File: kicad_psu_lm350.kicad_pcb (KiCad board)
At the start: 2 copper layers, 28 parts, among them J1 AC Input, J2 AC Input, J3 DC +1.25 to +30V, J4 GND, J5 GND, J6 GND, J7 GND, U1 LM350_TO220

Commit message: Swapped pot pins, aligned schematic nets
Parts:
- moved D5 5.68 mm to (223.5, 48.3), turned to 90 degrees
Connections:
- C3 pad 2: Net-(C3-Pad2) -> Net-(C4-Pad1)
- C4 pad 1: Net-(C3-Pad2) -> Net-(C4-Pad1)
- D6 pad 2: Net-(C3-Pad2) -> Net-(C4-Pad1)
- R1 pad 2: Net-(C3-Pad2) -> Net-(C4-Pad1)
- R2 pad 1: Net-(C3-Pad2) -> Net-(C1-Pad2)
- R2 pad 3: Net-(C1-Pad2) -> Net-(C4-Pad1)
- U1 pad 1: Net-(C3-Pad2) -> Net-(C4-Pad1)
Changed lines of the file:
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@@
   (net 0 "")
   (net 1 "Net-(C5-Pad1)")
-  (net 2 "Net-(C3-Pad2)")
+  (net 2 "Net-(C4-Pad1)")
   (net 3 "Net-(C1-Pad2)")
   (net 4 "Net-(C1-Pad1)")
@@
     (fp_circle (center 1.25 0) (end 3.75 0) (layer "F.Fab") (width 0.1) (fill none))
     (pad "1" thru_hole rect (at 0 0) (size 1.6 1.6) (drill 0.8) (layers *.Cu *.Mask)
-      (net 2 "Net-(C3-Pad2)") (pintype "passive"))
+      (net 2 "Net-(C4-Pad1)") (pintype "passive"))
     (pad "2" thru_hole circle (at 2.5 0) (size 1.6 1.6) (drill 0.8) (layers *.Cu *.Mask)
       (net 3 "Net-(C1-Pad2)") (pintype "passive"))
@@
       (net 4 "Net-(C1-Pad1)") (pintype "passive"))
     (pad "2" thru_hole circle (at 5 0 180) (size 2 2) (drill 1) (layers *.Cu *.Mask)
-      (net 2 "Net-(C3-Pad2)") (pintype "passive"))
+      (net 2 "Net-(C4-Pad1)") (pintype "passive"))
     (model "${KICAD6_3DMODEL_DIR}/Capacitor_THT.3dshapes/C_Disc_D8.0mm_W5.0mm_P5.00mm.wrl"
       (offset (xyz 0 0 0))
@@
       (net 1 "Net-(C5-Pad1)") (pintype "passive"))
     (pad "2" thru_hole oval (at 10.16 0 270) (size 1.6 1.6) (drill 0.8) (layers *.Cu *.Mask)
-      (net 2 "Net-(C3-Pad2)") (pintype "passive"))
+      (net 2 "Net-(C4-Pad1)") (pintype "passive"))
     (model "${KICAD6_3DMODEL_DIR}/Resistor_THT.3dshapes/R_Axial_DIN0207_L6.3mm_D2.5mm_P10.16mm_Horizontal.wrl"
       (offset (xyz 0 0 0))
@@
     (fp_line (start -2.46 -3.15) (end -2.46 1.25) (layer "F.Fab") (width 0.1))
     (pad "1" thru_hole rect (at 0 0) (size 1.905 2) (drill 1.1) (layers *.Cu *.Mask)
-      (net 2 "Net-(C3-Pad2)") (pinfunction "ADJ") (pintype "input"))
+      (net 2 "Net-(C4-Pad1)") (pinfunction "ADJ") (pintype "input"))
     (pad "2" thru_hole oval (at 2.54 0) (size 1.905 2) (drill 1.1) (layers *.Cu *.Mask)
       (net 1 "Net-(C5-Pad1)") (pinfunction "VO") (pintype "power_out"))
@@
   )
   (footprint "Diode_THT:D_DO-41_SOD81_P10.16mm_Horizontal" (layer "F.Cu")
-    (at 220.98 43.18)
+    (at 223.52 48.26 90)
     (descr "Diode, DO-41_SOD81 series, Axial, Horizontal, pin pitch=10.16mm, , length*diameter=5.2*2.7mm^2, , http://www.diodes.com/_files/packages/DO-41%20(Plastic).pdf")
     (tags "Diode DO-41_SOD81 series Axial Horizontal pin pitch 10.16mm  length 5.2mm diameter 2.7mm")
@@
     (property "Sheetname" "")
     (attr through_hole)
-    (fp_text reference "D5" (at 5.08 -2.47) (layer "F.SilkS")
-      (effects (font (size 1 1) (thickness 0.15)))
-    )
-    (fp_text value "1N4007" (at 5.08 2.47) (layer "F.Fab")
-      (effects (font (size 1 1) (thickness 0.15)))
-    )
-    (fp_text user "K" (at 0 -2.1) (layer "F.SilkS")
-      (effects (font (size 1 1) (thickness 0.15)))
-    )
-    (fp_text user "K" (at 0 -2.1) (layer "F.Fab")
-      (effects (font (size 1 1) (thickness 0.15)))
-    )
-    (fp_text user "${REFERENCE}" (at 5.47 0) (layer "F.Fab")
+    (fp_text reference "D5" (at 5.08 -2.47 90) (layer "F.SilkS")
+      (effects (font (size 1 1) (thickness 0.15)))
+    )
+    (fp_text value "1N4007" (at 5.08 2.47 90) (layer "F.Fab")
+      (effects (font (size 1 1) (thickness 0.15)))
+    )
+    (fp_text user "K" (at 0 -2.1 90) (layer "F.SilkS")
+      (effects (font (size 1 1) (thickness 0.15)))
+    )
+    (fp_text user "K" (at 0 -2.1 90) (layer "F.Fab")
+      (effects (font (size 1 1) (thickness 0.15)))
+    )
+    (fp_text user "${REFERENCE}" (at 5.47 0 90) (layer "F.Fab")
       (effects (font (size 1 1) (thickness 0.15)))
     )
@@
     (fp_line (start 10.16 0) (end 7.68 0) (layer "F.Fab") (width 0.1))
     (fp_line (start 3.36 -1.35) (end 3.36 1.35) (layer "F.Fab") (width 0.1))
-    (pad "1" thru_hole rect (at 0 0) (size 2.2 2.2) (drill 1.1) (layers *.Cu *.Mask)
+    (pad "1" thru_hole rect (at 0 0 90) (size 2.2 2.2) (drill 1.1) (layers *.Cu *.Mask)
       (net 4 "Net-(C1-Pad1)") (pinfunction "K") (pintype "passive"))
-    (pad "2" thru_hole oval (at 10.16 0) (size 2.2 2.2) (drill 1.1) (layers *.Cu *.Mask)
+    (pad "2" thru_hole oval (at 10.16 0 90) (size 2.2 2.2) (drill 1.1) (layers *.Cu *.Mask)
       (net 1 "Net-(C5-Pad1)") (pinfunction "A") (pintype "passive"))
     (model "${KICAD6_3DMODEL_DIR}/Diode_THT.3dshapes/D_DO-41_SOD81_P10.16mm_Horizontal.wrl"
@@
       (net 1 "Net-(C5-Pad1)") (pinfunction "K") (pintype "passive"))
     (pad "2" thru_hole oval (at 10.16 0 270) (size 2.2 2.2) (drill 1.1) (layers *.Cu *.Mask)
-      (net 2 "Net-(C3-Pad2)") (pinfunction "A") (pintype "passive"))
+      (net 2 "Net-(C4-Pad1)") (pinfunction "A") (pintype "passive"))
     (model "${KICAD6_3DMODEL_DIR}/Diode_THT.3dshapes/D_DO-41_SOD81_P10.16mm_Horizontal.wrl"
       (offset (xyz 0 0 0))
@@
     (fp_line (start -3.75 3.71) (end 5.08 3.71) (layer "F.Fab") (width 0.1))
     (pad "1" thru_hole circle (at 0 0 270) (size 1.8 1.8) (drill 1) (layers *.Cu *.Mask)
-      (net 2 "Net-(C3-Pad2)") (pinfunction "1") (pintype "passive"))
+      (net 3 "Net-(C1-Pad2)") (pinfunction "1") (pintype "passive"))
     (pad "2" thru_hole circle (at 0 -2.54 270) (size 1.8 1.8) (drill 1) (layers *.Cu *.Mask)
       (net 3 "Net-(C1-Pad2)") (pinfunction "2") (pintype "passive"))
     (pad "3" thru_hole circle (at 0 -5.08 270) (size 1.8 1.8) (drill 1) (layers *.Cu *.Mask)
-      (net 3 "Net-(C1-Pad2)") (pinfunction "3") (pintype "passive"))
+      (net 2 "Net-(C4-Pad1)") (pinfunction "3") (pintype "passive"))
     (model "${KICAD6_3DMODEL_DIR}/Potentiometer_THT.3dshapes/Potentiometer_Vishay_148-149_Single_Horizontal.wrl"
       (offset (xyz 0 0 0))

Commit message: C4 should be tantalum to filter HF noise
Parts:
- C4: value 10uF/50V -> 1uF/50V
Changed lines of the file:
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@@
     (descr "CP, Radial series, Radial, pin pitch=2.50mm, , diameter=5mm, Electrolytic Capacitor")
     (tags "CP Radial series Radial pin pitch 2.50mm  diameter 5mm Electrolytic Capacitor")
+    (property "Cap Type" "tantalum")
     (property "Sheetfile" "kicad_psu_lm350.kicad_sch")
     (property "Sheetname" "")
@@
       (effects (font (size 1 1) (thickness 0.15)))
     )
-    (fp_text value "10uF/50V" (at 1.25 3.75) (layer "F.Fab")
+    (fp_text value "1uF/50V" (at 1.25 3.75) (layer "F.Fab")
       (effects (font (size 1 1) (thickness 0.15)))
     )

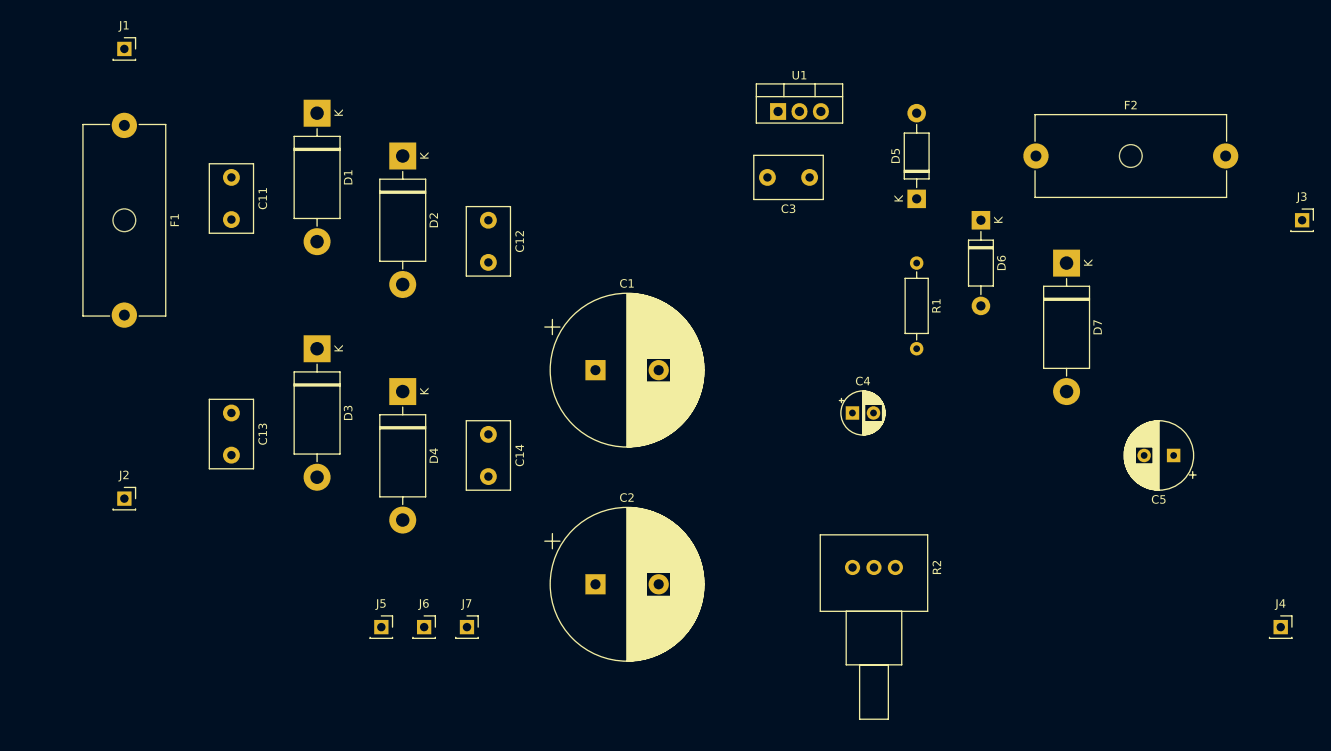
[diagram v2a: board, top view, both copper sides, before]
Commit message: Upgraded to KiCad7, board outline, mounting holes
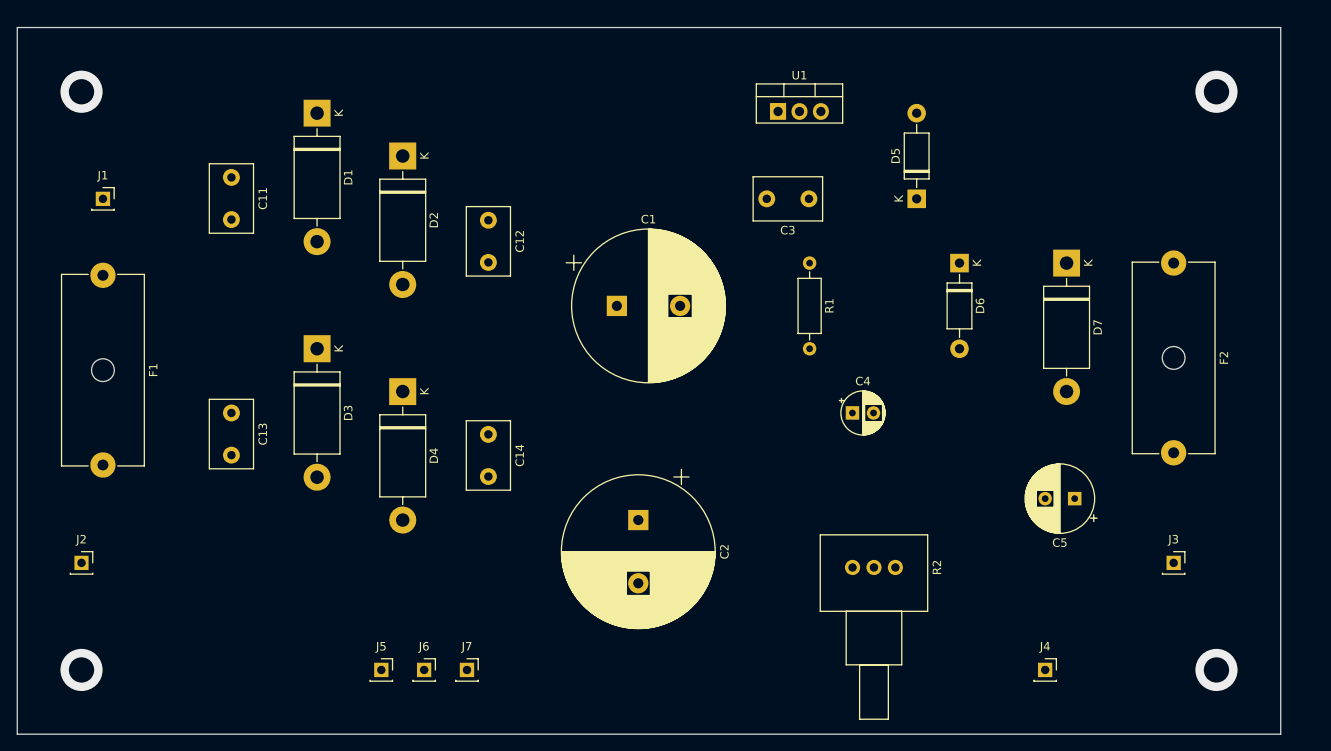
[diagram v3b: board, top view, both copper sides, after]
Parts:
- moved J3 43.4 mm to (254.0, 91.4)
- moved J4 28.4 mm to (238.8, 104.1)
- moved F2 20.7 mm to (254.0, 55.9), turned to -90 degrees
- moved F1 18.0 mm to (127.0, 57.3)
- moved J1 18.0 mm to (127.0, 48.3)
- moved C5 12.8 mm to (242.3, 83.8)
- moved R1 12.7 mm to (210.8, 55.9)
- moved C2 9.16 mm to (190.5, 86.4), turned to -90 degrees
- moved J2 9.16 mm to (124.5, 91.4)
- moved C1 8.03 mm to (188.0, 61.0)
- moved D6 5.68 mm to (228.6, 55.9)
- moved J5 5.08 mm to (160.0, 104.1)
- moved J6 5.08 mm to (165.1, 104.1)
- moved J7 5.08 mm to (170.2, 104.1)
- moved C3 2.54 mm to (210.7, 48.3)
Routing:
- net (no net): vias 0 -> 4
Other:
- board outline added: 149.9 x 83.8 mm

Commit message: First routed version
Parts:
- moved J6 25.5 mm to (190.5, 106.7)
- moved J7 25.5 mm to (195.6, 106.7)
- moved J5 25.5 mm to (185.4, 106.7)
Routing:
- net Net-(C1-Pad2): track 0.00 -> 224.9 mm
- net Net-(C1-Pad1): track 0.00 -> 137.4 mm
- net Net-(C5-Pad1): track 0.00 -> 114.6 mm
- net Net-(C12-Pad2): track 0.00 -> 87.2 mm
- net Net-(C4-Pad1): track 0.00 -> 80.7 mm
- net Net-(C11-Pad2): track 0.00 -> 55.1 mm
- net Net-(F2-Pad2): track 0.00 -> 13.1 mm
- net Net-(F1-Pad1): track 0.00 -> 9.07 mm
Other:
- board text added: "GitHub.com/hpaluch/kicad_psu_lm350"
- board text added: "PSU w LM350"
